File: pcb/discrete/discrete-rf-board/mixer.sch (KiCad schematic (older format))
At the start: 63 parts

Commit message: Save changes while moving over to the new laptop
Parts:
- removed C? (x6): 100 pF, symbol Device:C_Small
- removed C?: 1.2 pF, symbol Device:C_Small
- removed C?: 1 nF, symbol Device:C_Small
- removed C? (x2): 33 nF, symbol Device:C_Small
- removed L?: 31 nH, symbol Device:L_Small
- removed L? (x2): 680 nH, symbol Device:L_Small
- removed L? (x2): 27 nH, symbol Device:L_Small
- removed L? (x2): 12 nH, symbol Device:L_Small
- removed L? (x2): 470 uH, symbol Device:L_Small
- removed Q? (x4): BFU520XRR, symbol discrete-parts:Q_NPN_BCEE
- removed Q? (x4): Q_NPN_BCE, symbol Device:Q_NPN_BCE
- removed R?: 220R, symbol Device:R_Small
- removed R? (x2): 2k, symbol Device:R_Small
- removed R? (x2): 3k, symbol Device:R_Small
- removed R? (x4): 33R, symbol Device:R_Small
- removed R? (x2): 3.3R, symbol Device:R_Small
- removed R? (x5): 1k, symbol Device:R_Small
- removed R? (x5): 33R 1%, symbol Device:R_Small
- removed R?: 390R, symbol Device:R_Small
- removed TP? (x4): TestPoint, symbol Connector:TestPoint
- added U?: LT5560EDD#PBF, symbol discrete-parts:LT5560EDD#PBF
- gave numbers to parts that had none: 10
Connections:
- wire segments 193 -> 42
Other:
- note removed: "Should see about -2 dBm LO drive after balun"
- note removed: "TODO source NPNs"
- note removed: "Third harmonic is 15 dB down from fundamental"
- moved on the sheet: R801, U801

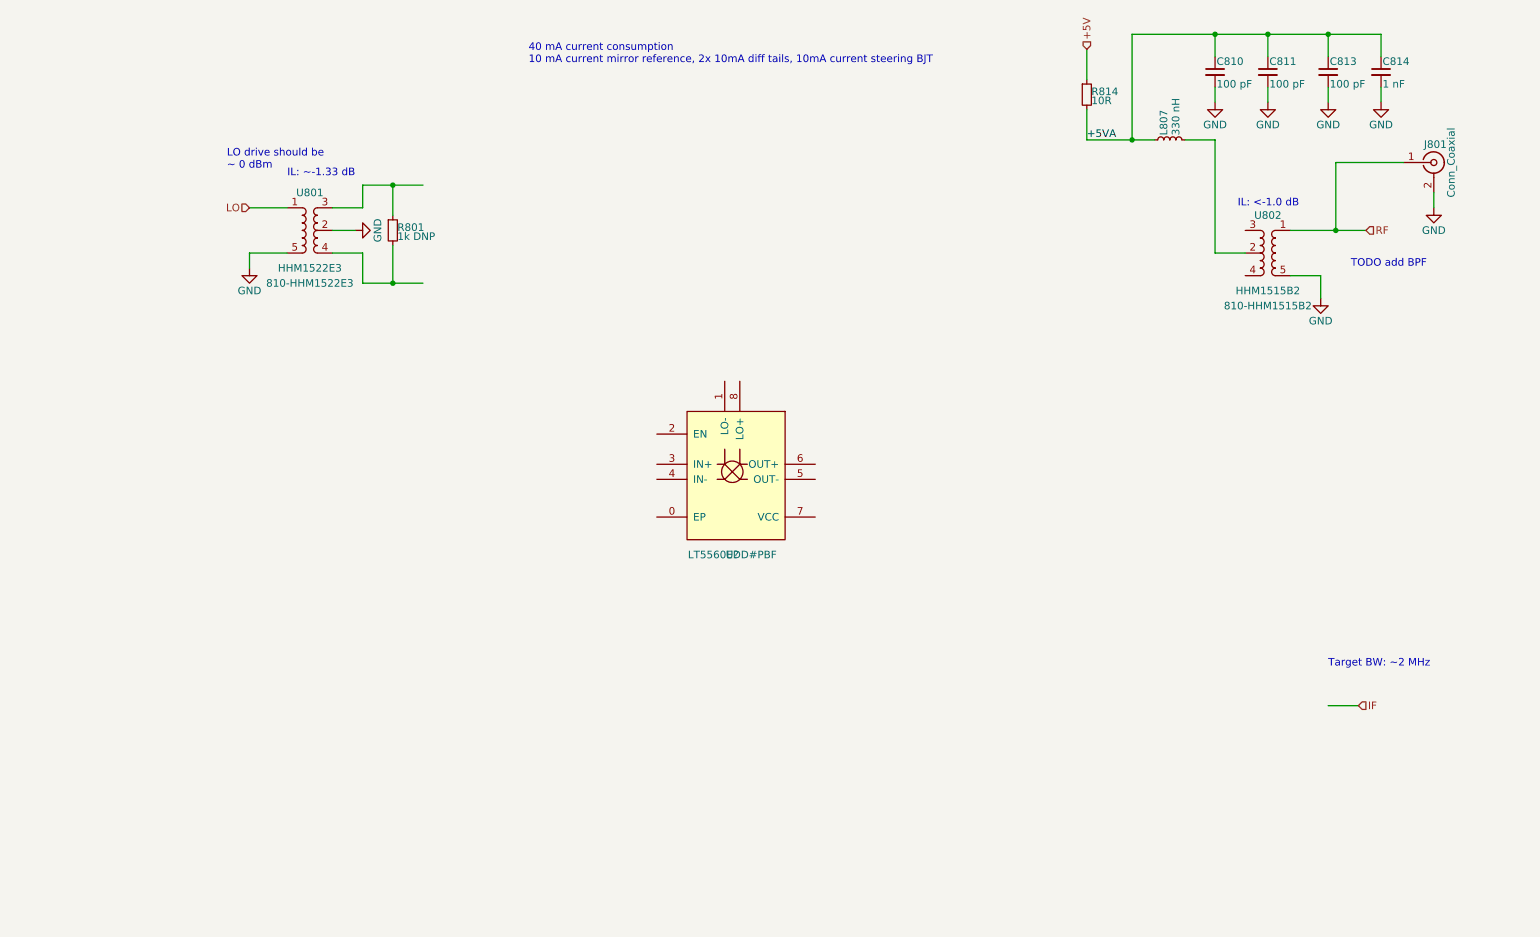
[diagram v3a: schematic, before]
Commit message: Finish TX mixer; added IF buffer
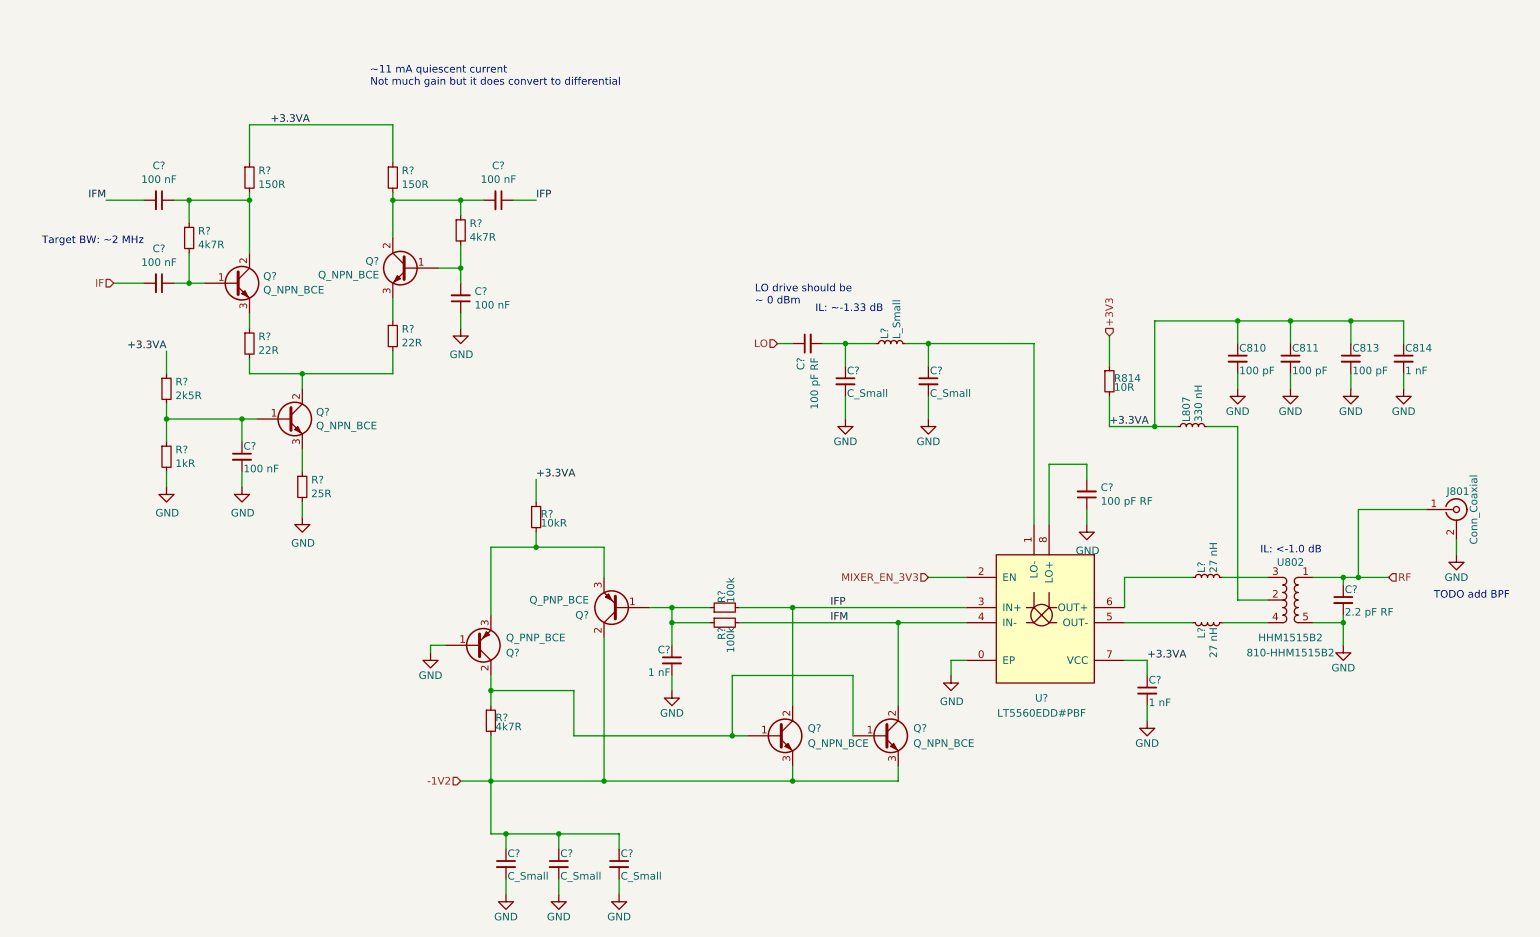
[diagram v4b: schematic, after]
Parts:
- removed R801: 1k DNP, symbol Device:R_Small
- removed U801: HHM1522E3, symbol discrete-parts:HHM1522E3
- added C? (x2): 100 pF RF, symbol Device:C_Small
- added C? (x5): C_Small, symbol Device:C_Small
- added C? (x2): 1 nF, symbol Device:C_Small
- added C?: 2.2 pF RF, symbol Device:C_Small
- added C? (x5): 100 nF, symbol Device:C_Small
- added L?: L_Small, symbol Device:L_Small
- added L? (x2): 27 nH, symbol Device:L_Small
- added Q? (x5): Q_NPN_BCE, symbol Device:Q_NPN_BCE
- added Q? (x2): Q_PNP_BCE, symbol Device:Q_PNP_BCE
- added R? (x2): 100k, symbol Device:R_Small
- added R? (x2): 22R, symbol Device:R_Small
- added R? (x2): 150R, symbol Device:R_Small
- added R? (x3): 4k7R, symbol Device:R_Small
- added R?: 25R, symbol Device:R_Small
- added R?: 2k5R, symbol Device:R_Small
- added R?: 1kR, symbol Device:R_Small
- added R?: 10kR, symbol Device:R_Small
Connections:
- net labels added: +3.3VA, +3V3, -1V2, IFM, IFP, MIXER_EN_3V3
- net labels removed: +5V, +5VA
- wire segments 42 -> 142
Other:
- note added: "~~11 mA quiescent current\nNot much gain but it does convert to differential"
- note removed: "40 mA current consumption\n10 mA current mirror reference, 2x 10mA diff tails, 10mA current steering BJT"
- moved on the sheet: C810, C811, C813, C814, J801, L807, R814, U802, U?

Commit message: Merge stuff I guess, hopefully this doesn't break too much
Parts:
- removed R? (x2): 150R, symbol Device:R_Small
- removed U802: HHM1515B2, symbol discrete-parts:HHM1515B2
- added Q? (x2): Q_PNP_BCE, symbol Device:Q_PNP_BCE
- added R? (x2): 1kR, symbol Device:R_Small
- added T?: HHM1515B2, symbol discrete-parts:HHM1515B2
- gave numbers to parts that had none: 37
- renumbered C810 to C1415, C811 to C1416, C813 to C1418, C814 to C1419, J801 to J1401, L807 to L1402, R814 to R1414
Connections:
- net +3.3VA: now also Q?.3 (E), Q?.3 (E)
- net GND: now also T?.5 (GND)
- net RF: now also T?.1 (SINGLE)
- net at L1402.2: now also T?.2 (COMMON)
- net at L1403.2: now also T?.3 (+)
- net at L1404.2: now also T?.4 (-)
- net at C1401.1, Q1401.2 (C), R1403.1: now also Q?.2 (C), R?.2
- net at C1405.2, Q1403.2 (C), R1409.1: now also Q?.2 (C), R?.1
- new net: Q?.1 (B), Q?.1 (B), R?.1, R?.2
